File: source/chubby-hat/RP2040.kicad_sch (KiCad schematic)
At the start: 23 parts, among them U4 P25Q40H-SSH-IT, U5 RP2040, Y1 12M

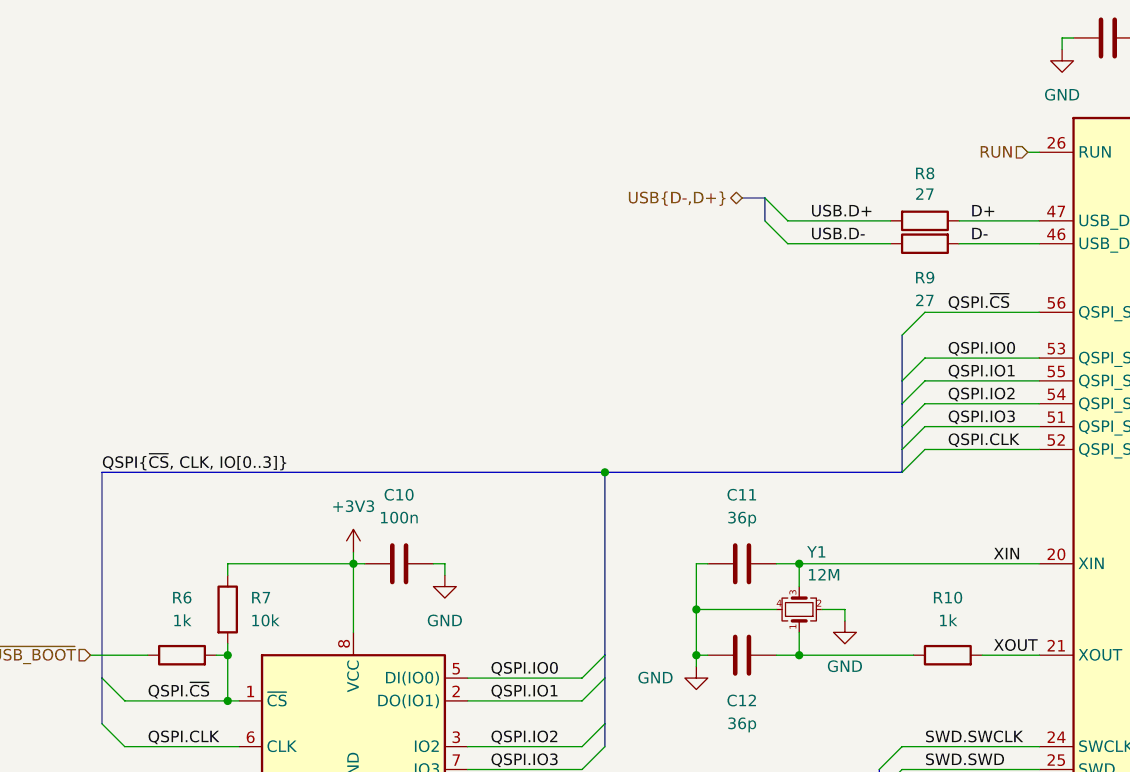
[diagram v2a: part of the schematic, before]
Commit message: add zero volt diodes to USB and modules; add status LEDs; add RP2040 SWD - closes #9
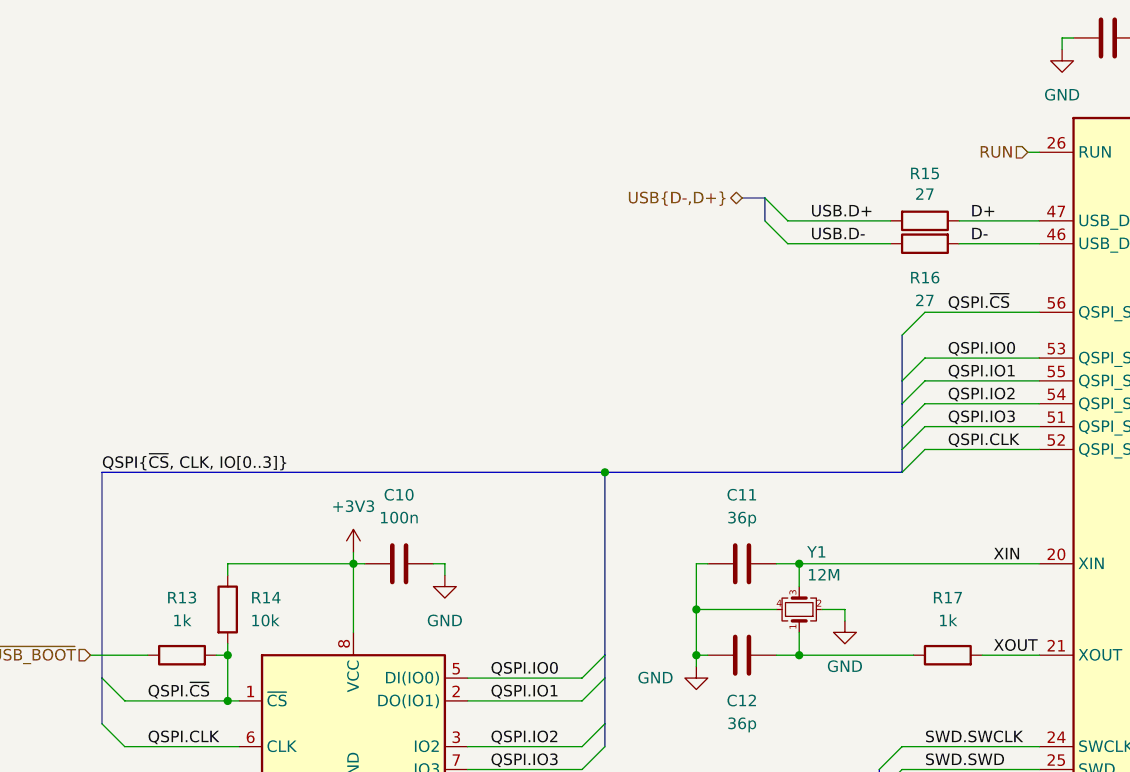
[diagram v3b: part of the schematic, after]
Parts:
- renumbered R6 to R13, R7 to R14, R8 to R15, R9 to R16, R10 to R17
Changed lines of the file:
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@@
   (symbol (lib_id "power:GND") (at 241.3 36.83 0) (unit 1)
     (in_bom yes) (on_board yes) (fields_autoplaced)
-    (property "Reference" "#PWR096" (id 0) (at 241.3 43.18 0)
+    (property "Reference" "#PWR0103" (id 0) (at 241.3 43.18 0)
       (effects (font (size 1.27 1.27)) hide)
     )
@@
   (symbol (lib_id "power:+3V3") (at 68.58 113.03 0) (unit 1)
     (in_bom yes) (on_board yes) (fields_autoplaced)
-    (property "Reference" "#PWR085" (id 0) (at 68.58 116.84 0)
+    (property "Reference" "#PWR092" (id 0) (at 68.58 116.84 0)
       (effects (font (size 1.27 1.27)) hide)
     )
@@
   (symbol (lib_id "power:GND") (at 68.58 143.51 0) (unit 1)
     (in_bom yes) (on_board yes) (fields_autoplaced)
-    (property "Reference" "#PWR086" (id 0) (at 68.58 149.86 0)
+    (property "Reference" "#PWR093" (id 0) (at 68.58 149.86 0)
       (effects (font (size 1.27 1.27)) hide)
     )
@@
   (symbol (lib_id "power:GND") (at 147.32 57.15 0) (unit 1)
     (in_bom yes) (on_board yes) (fields_autoplaced)
-    (property "Reference" "#PWR091" (id 0) (at 147.32 63.5 0)
+    (property "Reference" "#PWR098" (id 0) (at 147.32 63.5 0)
       (effects (font (size 1.27 1.27)) hide)
     )
@@
   (symbol (lib_id "power:GND") (at 152.4 36.83 0) (unit 1)
     (in_bom yes) (on_board yes) (fields_autoplaced)
-    (property "Reference" "#PWR092" (id 0) (at 152.4 43.18 0)
+    (property "Reference" "#PWR099" (id 0) (at 152.4 43.18 0)
       (effects (font (size 1.27 1.27)) hide)
     )
@@
   (symbol (lib_id "power:GND") (at 78.74 115.57 0) (unit 1)
     (in_bom yes) (on_board yes) (fields_autoplaced)
-    (property "Reference" "#PWR087" (id 0) (at 78.74 121.92 0)
+    (property "Reference" "#PWR094" (id 0) (at 78.74 121.92 0)
       (effects (font (size 1.27 1.27)) hide)
     )
@@
   (symbol (lib_id "Device:R") (at 49.53 124.46 90) (unit 1)
     (in_bom yes) (on_board yes) (fields_autoplaced)
-    (property "Reference" "R6" (id 0) (at 49.53 118.11 90))
+    (property "Reference" "R13" (id 0) (at 49.53 118.11 90))
     (property "Value" "1k" (id 1) (at 49.53 120.65 90))
     (property "Footprint" "Resistor_SMD:R_0603_1608Metric" (id 2) (at 49.53 126.238 90)
@@
   (symbol (lib_id "power:+3V3") (at 175.26 24.13 0) (unit 1)
     (in_bom yes) (on_board yes) (fields_autoplaced)
-    (property "Reference" "#PWR094" (id 0) (at 175.26 27.94 0)
+    (property "Reference" "#PWR0101" (id 0) (at 175.26 27.94 0)
       (effects (font (size 1.27 1.27)) hide)
     )
@@
   (symbol (lib_id "Device:R") (at 134.62 124.46 90) (unit 1)
     (in_bom yes) (on_board yes) (fields_autoplaced)
-    (property "Reference" "R10" (id 0) (at 134.62 118.11 90))
+    (property "Reference" "R17" (id 0) (at 134.62 118.11 90))
     (property "Value" "1k" (id 1) (at 134.62 120.65 90))
     (property "Footprint" "Resistor_SMD:R_0603_1608Metric" (id 2) (at 134.62 126.238 90)
@@
   (symbol (lib_id "power:GND") (at 123.19 120.65 0) (unit 1)
     (in_bom yes) (on_board yes) (fields_autoplaced)
-    (property "Reference" "#PWR089" (id 0) (at 123.19 127 0)
+    (property "Reference" "#PWR096" (id 0) (at 123.19 127 0)
       (effects (font (size 1.27 1.27)) hide)
     )
@@
   (symbol (lib_id "power:GND") (at 170.18 153.67 0) (unit 1)
     (in_bom yes) (on_board yes) (fields_autoplaced)
-    (property "Reference" "#PWR093" (id 0) (at 170.18 160.02 0)
+    (property "Reference" "#PWR0100" (id 0) (at 170.18 160.02 0)
       (effects (font (size 1.27 1.27)) hide)
     )
@@
   (symbol (lib_id "power:GND") (at 198.12 57.15 0) (unit 1)
     (in_bom yes) (on_board yes) (fields_autoplaced)
-    (property "Reference" "#PWR095" (id 0) (at 198.12 63.5 0)
+    (property "Reference" "#PWR0102" (id 0) (at 198.12 63.5 0)
       (effects (font (size 1.27 1.27)) hide)
     )
@@
   (symbol (lib_id "power:GND") (at 106.68 125.73 0) (unit 1)
     (in_bom yes) (on_board yes) (fields_autoplaced)
-    (property "Reference" "#PWR088" (id 0) (at 106.68 132.08 0)
+    (property "Reference" "#PWR095" (id 0) (at 106.68 132.08 0)
       (effects (font (size 1.27 1.27)) hide)
     )
@@
   (symbol (lib_id "Device:R") (at 132.08 76.2 270) (unit 1)
     (in_bom yes) (on_board yes)
-    (property "Reference" "R8" (id 0) (at 132.08 70.9738 90))
+    (property "Reference" "R15" (id 0) (at 132.08 70.9738 90))
     (property "Value" "27" (id 1) (at 132.08 73.2725 90))
     (property "Footprint" "Resistor_SMD:R_0603_1608Metric" (id 2) (at 132.08 74.422 90)
@@
   (symbol (lib_id "Device:R") (at 132.08 78.74 90) (mirror x) (unit 1)
     (in_bom yes) (on_board yes)
-    (property "Reference" "R9" (id 0) (at 132.08 82.55 90))
+    (property "Reference" "R16" (id 0) (at 132.08 82.55 90))
     (property "Value" "27" (id 1) (at 132.08 85.09 90))
     (property "Footprint" "Resistor_SMD:R_0603_1608Metric" (id 2) (at 132.08 76.962 90)
@@
   (symbol (lib_id "Device:R") (at 54.61 119.38 0) (unit 1)
     (in_bom yes) (on_board yes) (fields_autoplaced)
-    (property "Reference" "R7" (id 0) (at 57.15 118.1099 0)
+    (property "Reference" "R14" (id 0) (at 57.15 118.1099 0)
       (effects (font (size 1.27 1.27)) (justify left))
     )
@@
   (symbol (lib_id "power:GND") (at 142.24 146.05 0) (unit 1)
     (in_bom yes) (on_board yes) (fields_autoplaced)
-    (property "Reference" "#PWR090" (id 0) (at 142.24 152.4 0)
-      (effects (font (size 1.27 1.27)) hide)
-    )
+    (property "Reference" "#PWR097" (id 0) (at 142.24 152.4 0)
+      (effects (font (size 1.27 1.27)) hide)
+    )

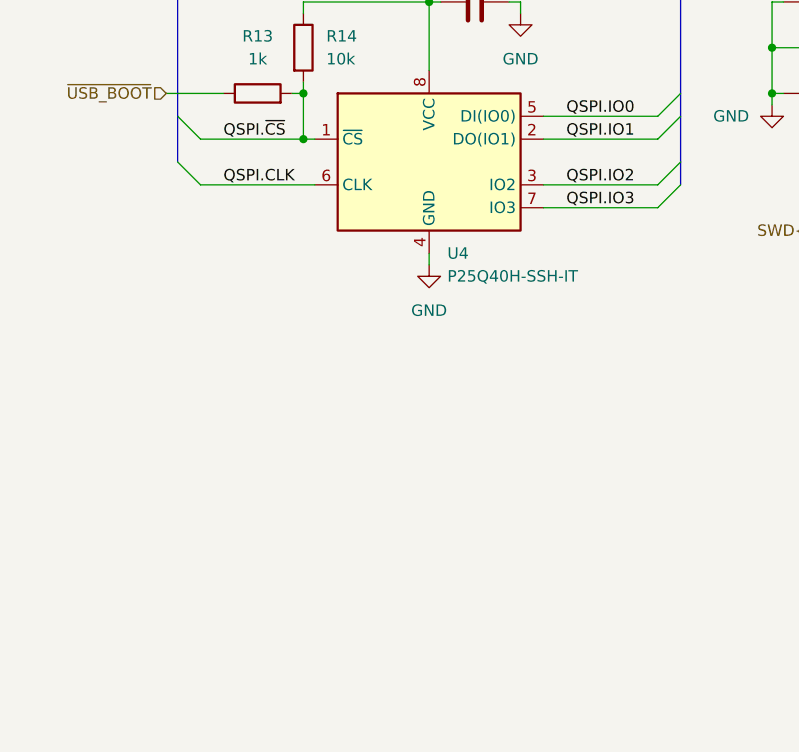
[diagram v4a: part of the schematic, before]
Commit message: add USON-8 footprint for W25Q16JV style flash; closes #13
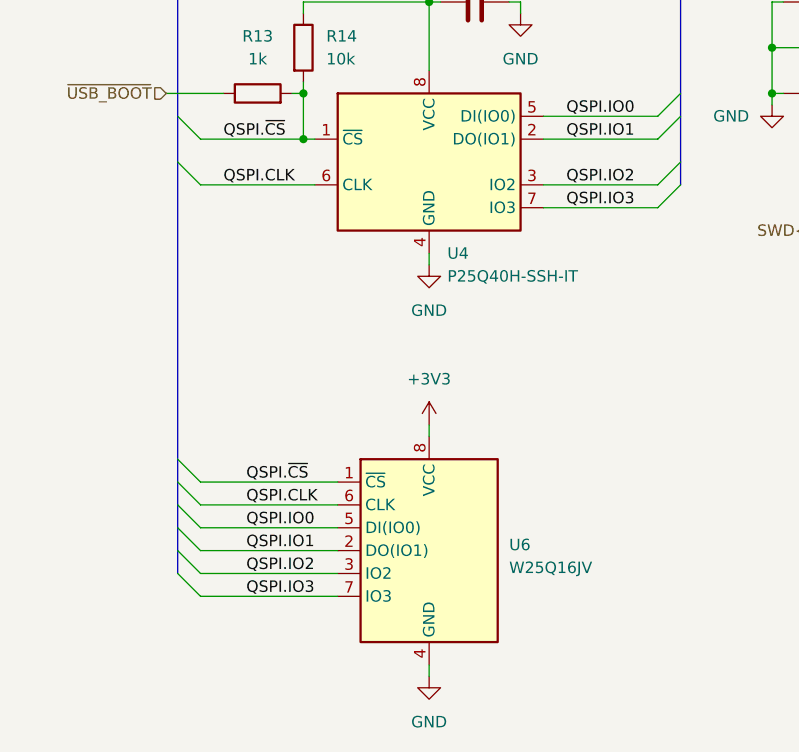
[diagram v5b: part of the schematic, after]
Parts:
- added U6: W25Q16JV, Package_SO:VSSOP-8_2.3x2mm_P0.5mm, symbol Memory_Flash:W25Q32JVSS
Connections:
- net +3V3: now also U6.8 (VCC)
- net GND: now also U6.4 (GND)
- net QSPI.CLK: now also U6.6 (CLK)
- net QSPI.IO0: now also U6.5 (DI(IO0))
- net QSPI.IO1: now also U6.2 (DO(IO1))
- net QSPI.IO2: now also U6.3 (IO2)
- net QSPI.IO3: now also U6.7 (IO3)
- net QSPI.~{CS}: now also U6.1 (~{CS})
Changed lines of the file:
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@@
+    (stroke (width 0) (type default))
+  )
+  (bus_entry (at 40.64 175.26) (size 2.54 2.54)
     (stroke (width 0) (type default))
   )
@@
     (stroke (width 0) (type default))
   )
+  (bus_entry (at 40.64 167.64) (size 2.54 2.54)
+    (stroke (width 0) (type default))
+  )
   (bus_entry (at 114.3 76.2) (size 2.54 2.54)
     (stroke (width 0) (type default))
@@
     (stroke (width 0) (type default))
   )
+  (bus_entry (at 40.64 172.72) (size 2.54 2.54)
+    (stroke (width 0) (type default))
+  )
   (bus_entry (at 40.64 127) (size 2.54 2.54)
     (stroke (width 0) (type default))
@@
     (stroke (width 0) (type default))
   )
+  (bus_entry (at 40.64 165.1) (size 2.54 2.54)
+    (stroke (width 0) (type default))
+  )
   (bus_entry (at 210.82 111.76) (size -2.54 2.54)
     (stroke (width 0) (type default))
@@
     (stroke (width 0) (type default))
   )
+  (bus_entry (at 40.64 170.18) (size 2.54 2.54)
+    (stroke (width 0) (type default))
+  )
   (bus_entry (at 210.82 96.52) (size -2.54 2.54)
     (stroke (width 0) (type default))
@@
     (stroke (width 0) (type default))
   )
+  (bus_entry (at 40.64 177.8) (size 2.54 2.54)
+    (stroke (width 0) (type default))
+  )
   (bus_entry (at 210.82 114.3) (size -2.54 2.54)
     (stroke (width 0) (type default))
@@
     (stroke (width 0) (type default))
   )
+  (wire (pts (xy 43.18 175.26) (xy 58.42 175.26))
+    (stroke (width 0) (type default))
+  )
   (wire (pts (xy 195.58 144.78) (xy 208.28 144.78))
     (stroke (width 0) (type default))
@@
     (stroke (width 0) (type default))
   )
+  (bus (pts (xy 40.64 167.64) (xy 40.64 170.18))
+    (stroke (width 0) (type default))
+  )
   (bus (pts (xy 96.52 104.14) (xy 96.52 124.46))
     (stroke (width 0) (type default))
@@
     (stroke (width 0) (type default))
   )
+  (wire (pts (xy 68.58 161.29) (xy 68.58 162.56))
+    (stroke (width 0) (type default))
+  )
   (wire (pts (xy 195.58 106.68) (xy 208.28 106.68))
     (stroke (width 0) (type default))
@@
     (stroke (width 0) (type default))
   )
+  (bus (pts (xy 40.64 172.72) (xy 40.64 175.26))
+    (stroke (width 0) (type default))
+  )
   (wire (pts (xy 203.2 25.4) (xy 203.2 26.67))
     (stroke (width 0) (type default))
@@
     (stroke (width 0) (type default))
   )
+  (wire (pts (xy 68.58 187.96) (xy 68.58 189.23))
+    (stroke (width 0) (type default))
+  )
   (wire (pts (xy 54.61 129.54) (xy 55.88 129.54))
     (stroke (width 0) (type default))
@@
     (stroke (width 0) (type default))
   )
+  (bus (pts (xy 40.64 165.1) (xy 40.64 167.64))
+    (stroke (width 0) (type default))
+  )
   (bus (pts (xy 129.54 93.98) (xy 129.54 96.52))
     (stroke (width 0) (type default))
@@
     (stroke (width 0) (type default))
   )
+  (wire (pts (xy 43.18 177.8) (xy 58.42 177.8))
+    (stroke (width 0) (type default))
+  )
   (wire (pts (xy 132.08 93.98) (xy 144.78 93.98))
     (stroke (width 0) (type default))
@@
     (stroke (width 0) (type default))
   )
+  (wire (pts (xy 43.18 180.34) (xy 58.42 180.34))
+    (stroke (width 0) (type default))
+  )
   (wire (pts (xy 195.58 139.7) (xy 208.28 139.7))
     (stroke (width 0) (type default))
@@
     (stroke (width 0) (type default))
   )
+  (wire (pts (xy 43.18 172.72) (xy 58.42 172.72))
+    (stroke (width 0) (type default))
+  )
   (bus (pts (xy 210.82 101.6) (xy 210.82 104.14))
     (stroke (width 0) (type default))
@@
   )
   (wire (pts (xy 177.8 25.4) (xy 190.5 25.4))
+    (stroke (width 0) (type default))
+  )
+  (wire (pts (xy 43.18 167.64) (xy 58.42 167.64))
     (stroke (width 0) (type default))
   )
@@
     (stroke (width 0) (type default))
   )
+  (bus (pts (xy 40.64 132.08) (xy 40.64 165.1))
+    (stroke (width 0) (type default))
+  )
   (wire (pts (xy 132.08 86.36) (xy 144.78 86.36))
     (stroke (width 0) (type default))
@@
     (stroke (width 0) (type default))
   )
+  (bus (pts (xy 40.64 175.26) (xy 40.64 177.8))
+    (stroke (width 0) (type default))
+  )
   (wire (pts (xy 118.11 124.46) (xy 130.81 124.46))
     (stroke (width 0) (type default))
@@
     (stroke (width 0) (type default))
   )
+  (wire (pts (xy 43.18 170.18) (xy 58.42 170.18))
+    (stroke (width 0) (type default))
+  )
   (wire (pts (xy 116.84 78.74) (xy 128.27 78.74))
     (stroke (width 0) (type default))
@@
   )
   (wire (pts (xy 107.95 114.3) (xy 106.68 114.3))
+    (stroke (width 0) (type default))
+  )
+  (bus (pts (xy 40.64 170.18) (xy 40.64 172.72))
     (stroke (width 0) (type default))
   )
@@
     (effects (font (size 1.27 1.27)) (justify left bottom))
   )
+  (label "QSPI.IO2" (at 48.26 177.8 0) (fields_autoplaced)
+    (effects (font (size 1.27 1.27)) (justify left bottom))
+  )
   (label "VREG_OUT" (at 165.1 55.88 180) (fields_autoplaced)
     (effects (font (size 1.27 1.27)) (justify right bottom))
@@
     (effects (font (size 1.27 1.27)) (justify left bottom))
   )
+  (label "QSPI.IO0" (at 48.26 172.72 0) (fields_autoplaced)
+    (effects (font (size 1.27 1.27)) (justify left bottom))
+  )
   (label "GPIO12" (at 198.12 99.06 0) (fields_autoplaced)
     (effects (font (size 1.27 1.27)) (justify left bottom))
@@
     (effects (font (size 1.27 1.27)) (justify left bottom))
   )
+  (label "QSPI.CLK" (at 48.26 170.18 0) (fields_autoplaced)
+    (effects (font (size 1.27 1.27)) (justify left bottom))
+  )
   (label "QSPI.~{CS}" (at 45.72 129.54 0) (fields_autoplaced)
     (effects (font (size 1.27 1.27)) (justify left bottom))
   )
+  (label "QSPI.IO3" (at 48.26 180.34 0) (fields_autoplaced)
+    (effects (font (size 1.27 1.27)) (justify left bottom))
+  )
   (label "GPIO27" (at 198.12 139.7 0) (fields_autoplaced)
     (effects (font (size 1.27 1.27)) (justify left bottom))
@@
     (effects (font (size 1.27 1.27)) (justify left bottom))
   )
+  (label "QSPI.~{CS}" (at 48.26 167.64 0) (fields_autoplaced)
+    (effects (font (size 1.27 1.27)) (justify left bottom))
+  )
   (label "GPIO29" (at 198.12 144.78 0) (fields_autoplaced)
     (effects (font (size 1.27 1.27)) (justify left bottom))
@@
   )
   (label "QSPI.IO3" (at 134.62 99.06 0) (fields_autoplaced)
+    (effects (font (size 1.27 1.27)) (justify left bottom))
+  )
+  (label "QSPI.IO1" (at 48.26 175.26 0) (fields_autoplaced)
     (effects (font (size 1.27 1.27)) (justify left bottom))
   )
@@
         (path "/4807f255-cede-4a86-b009-c3f93cadbbb8/e072f2d0-1d9f-486d-9f7d-b187c6021c47"
           (reference "#PWR0103") (unit 1)
+        )
+      )
+    )
+  )
+  (symbol (lib_id "power:+3V3") (at 68.58 161.29 0) (unit 1)
+    (in_bom yes) (on_board yes) (dnp no) (fields_autoplaced)
+    (property "Reference" "#PWR0104" (at 68.58 165.1 0)
+      (effects (font (size 1.27 1.27)) hide)
+    )
+    (property "Value" "+3V3" (at 68.58 156.21 0)
+      (effects (font (size 1.27 1.27)))
+    )
+    (property "Footprint" "" (at 68.58 161.29 0)
+      (effects (font (size 1.27 1.27)) hide)
+    )
+    (property "Datasheet" "" (at 68.58 161.29 0)
+      (effects (font (size 1.27 1.27)) hide)
+    )
+    (pin "1")
+    (instances
+      (project "chubby-hat"
+        (path "/4807f255-cede-4a86-b009-c3f93cadbbb8/e072f2d0-1d9f-486d-9f7d-b187c6021c47"
+          (reference "#PWR0104") (unit 1)
         )
       )
@@
     )
   )
+  (symbol (lib_id "power:GND") (at 68.58 189.23 0) (unit 1)
+    (in_bom yes) (on_board yes) (dnp no) (fields_autoplaced)
+    (property "Reference" "#PWR0105" (at 68.58 195.58 0)
+      (effects (font (size 1.27 1.27)) hide)
+    )
+    (property "Value" "GND" (at 68.58 194.31 0)
+      (effects (font (size 1.27 1.27)))
+    )
+    (property "Footprint" "" (at 68.58 189.23 0)
+      (effects (font (size 1.27 1.27)) hide)
+    )
+    (property "Datasheet" "" (at 68.58 189.23 0)
+      (effects (font (size 1.27 1.27)) hide)
+    )
+    (pin "1")
+    (instances
+      (project "chubby-hat"
+        (path "/4807f255-cede-4a86-b009-c3f93cadbbb8/e072f2d0-1d9f-486d-9f7d-b187c6021c47"
+          (reference "#PWR0105") (unit 1)
+        )
+      )
+    )
+  )
   (symbol (lib_id "Device:Crystal_GND24_Small") (at 118.11 119.38 90) (unit 1)
     (in_bom yes) (on_board yes) (dnp no) (fields_autoplaced)
@@
         )
       )
+    )
+  )
+  (symbol (lib_name "W25Q32JVSS_1") (lib_id "Memory_Flash:W25Q32JVSS") (at 68.58 175.26 0) (unit 1)
+    (in_bom yes) (on_board yes) (dnp no) (fields_autoplaced)
+    (property "Reference" "U6" (at 77.47 174.625 0)
+      (effects (font (size 1.27 1.27)) (justify left))
+    )
+    (property "Value" "W25Q16JV" (at 77.47 177.165 0)
+      (effects (font (size 1.27 1.27)) (justify left))
+    )
+    (property "Footprint" "Package_SO:VSSOP-8_2.3x2mm_P0.5mm" (at 68.58 175.26 0)
+      (effects (font (size 1.27 1.27)) hide)
+    )
+    (property "Datasheet" "http://www.winbond.com/resource-files/w25q32jv%20revg%2003272018%20plus.pdf" (at 68.58 175.26 0)
+      (effects (font (size 1.27 1.27)) hide)
+    )
+    (pin "1")
+    (pin "2")
+    (pin "3")
+    (pin "4")
+    (pin "5")
+    (pin "6")
+    (pin "7")
+    (pin "8")
+    (instances
+      (project "chubby-hat"
+        (path "/4807f255-cede-4a86-b009-c3f93cadbbb8/e072f2d0-1d9f-486d-9f7d-b187c6021c47"
+          (reference "U6") (unit 1)
+        )
+      )

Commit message: add prototyping area; closes #14
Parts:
- U5: LCSC (none) -> C2040; MPN (none) -> RP2040
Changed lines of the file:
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@@
+      (effects (font (size 1.27 1.27)) hide)
+    )
+    (property "LCSC" "C2040" (at 170.18 106.68 0)
+      (effects (font (size 1.27 1.27)) hide)
+    )
+    (property "MPN" "RP2040" (at 170.18 106.68 0)
       (effects (font (size 1.27 1.27)) hide)
     )
